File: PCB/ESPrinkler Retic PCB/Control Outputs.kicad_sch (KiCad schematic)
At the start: 0 parts

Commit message: Continue migrating PCB project to multi sheet design
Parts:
- added C1, C10, C11, C5, C6, C7, C8, C9: 12pF, symbol Device:C_Small
- added D1, D11, D14, D17, D22, D23, D24, D8: Generic_Triac_A1A2G, symbol Triac_Thyristor:Generic_Triac_A1A2G
- added D10, D13, D16, D19, D2, D20, D21, D7: D_TVS, symbol Device:D_TVS
- added D12, D15, D18, D25, D26, D27, D5, D9: LED, symbol Device:LED
- added Q1, Q10, Q4, Q5, Q6, Q7, Q8, Q9: Q_NMOS, symbol Device:Q_NMOS
- added R1, R17, R24, R31, R38, R49, R50, R51: 68R, symbol Device:R_Small
- added R15, R22, R29, R3, R36, R43, R44, R45: 120R, symbol Device:R_Small
- added R16, R2, R23, R30, R37, R46, R47, R48: 1.2k, symbol Device:R_Small
- added R18, R19, R25, R26, R32, R33, R39, R4, R40, R5, R52, R53, R54, R55, R56, R57: R, symbol Device:R
- added R20, R27, R34, R41, R58, R59, R6, R60: 10k, symbol Device:R
- added R21, R28, R35, R42, R61, R62, R63, R7: 1k, symbol Device:R
- added U1, U3, U4, U5, U6, U7, U8, U9: ~, symbol Relay_SolidState:MOC3063M
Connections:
- new net: D20.1 (A1), D23.2 (A2), R47.1
- new net: C10.1, R47.2, R50.1
- new net: D16.1 (A1), D17.2 (A2), R37.1
- new net: C11.1, R48.2, R51.1
- new net: C11.2, D24.1 (A1), R45.1
- new net: Q7.G, R41.2, R42.2
- new net: C9.2, D22.1 (A1), R43.1
- new net: D19.1 (A1), D22.2 (A2), R46.1
- new net: D22.3 (G), R43.2, U7.4
- new net: R19.2, U3.1
- new net: D18.2 (A), R39.2
- new net: Q10.G, R60.2, R63.2
- new net: R53.2, U7.1
- new net: D25.1 (K), Q8.S, U7.2
- new net: R49.2, U7.6
- new net: R33.2, U5.1
- new net: R40.2, U6.1
- new net: D18.1 (K), Q7.S, U6.2
- new net: D17.3 (G), R36.2, U6.4
- new net: R38.2, U6.6
- new net: D15.1 (K), Q6.S, U5.2
- new net: D14.3 (G), R29.2, U5.4
- new net: R31.2, U5.6
- new net: D12.2 (A), R25.2
- new net: C6.1, R23.2, R24.1
- new net: R24.2, U4.6
- new net: R4.2, U1.1
- new net: C6.2, D11.1 (A1), R22.1
- new net: D11.3 (G), R22.2, U4.4
- new net: D5.1 (K), Q1.S, U1.2
- new net: D1.3 (G), R3.2, U1.4
- new net: R1.2, U1.6
- new net: C10.2, D23.1 (A1), R44.1
- new net: Q4.G, R20.2, R21.2
- new net: D9.1 (K), Q4.S, U3.2
- new net: Q5.G, R27.2, R28.2
- new net: D7.1 (A1), D8.2 (A2), R16.1
- new net: C5.1, R16.2, R17.1
- new net: R51.2, U9.6
- new net: D23.3 (G), R44.2, U8.4
- new net: D27.1 (K), Q10.S, U9.2
- new net: D10.1 (A1), D11.2 (A2), R23.1
- new net: Q6.G, R34.2, R35.2
- new net: D1.2 (A2), D2.1 (A1), R2.1
- new net: C1.1, R1.1, R2.2
- new net: C9.1, R46.2, R49.1
- new net: C7.2, D14.1 (A1), R29.1
- new net: D13.1 (A1), D14.2 (A2), R30.1
- new net: Q1.G, R6.2, R7.2
- new net: R26.2, U4.1
- new net: Q8.G, R58.2, R61.2
- new net: D27.2 (A), R56.2
- new net: D26.1 (K), Q9.S, U8.2
- new net: D26.2 (A), R54.2
- new net: D15.2 (A), R32.2
- new net: D25.2 (A), R52.2
- new net: R57.2, U9.1
- new net: C5.2, D8.1 (A1), R15.1
- new net: D8.3 (G), R15.2, U3.4
- new net: C1.2, D1.1 (A1), R3.1
- new net: Q9.G, R59.2, R62.2
- new net: R55.2, U8.1
- new net: C7.1, R30.2, R31.1
- new net: D9.2 (A), R18.2
- new net: D5.2 (A), R5.2
- new net: D12.1 (K), Q5.S, U4.2
- new net: R17.2, U3.6
- new net: C8.1, R37.2, R38.1
- new net: R50.2, U8.6
- new net: C8.2, D17.1 (A1), R36.1
- new net: D21.1 (A1), D24.2 (A2), R48.1
- new net: D24.3 (G), R45.2, U9.4
- new net +5V: R18.1, R19.1, R25.1, R26.1, R32.1, R33.1, R39.1, R4.1, R40.1, R5.1, R52.1, R53.1, R54.1, R55.1, R56.1, R57.1
- new net GND: Q1.D, Q10.D, Q4.D, Q5.D, Q6.D, Q7.D, Q8.D, Q9.D, R20.1, R27.1, R34.1, R41.1, R58.1, R59.1, R6.1, R60.1
- new net LIVE: D10.2 (A2), D13.2 (A2), D16.2 (A2), D19.2 (A2), D2.2 (A2), D20.2 (A2), D21.2 (A2), D7.2 (A2)
- new net Pump: R21.1, R28.1, R35.1, R42.1, R61.1, R62.1, R63.1, R7.1

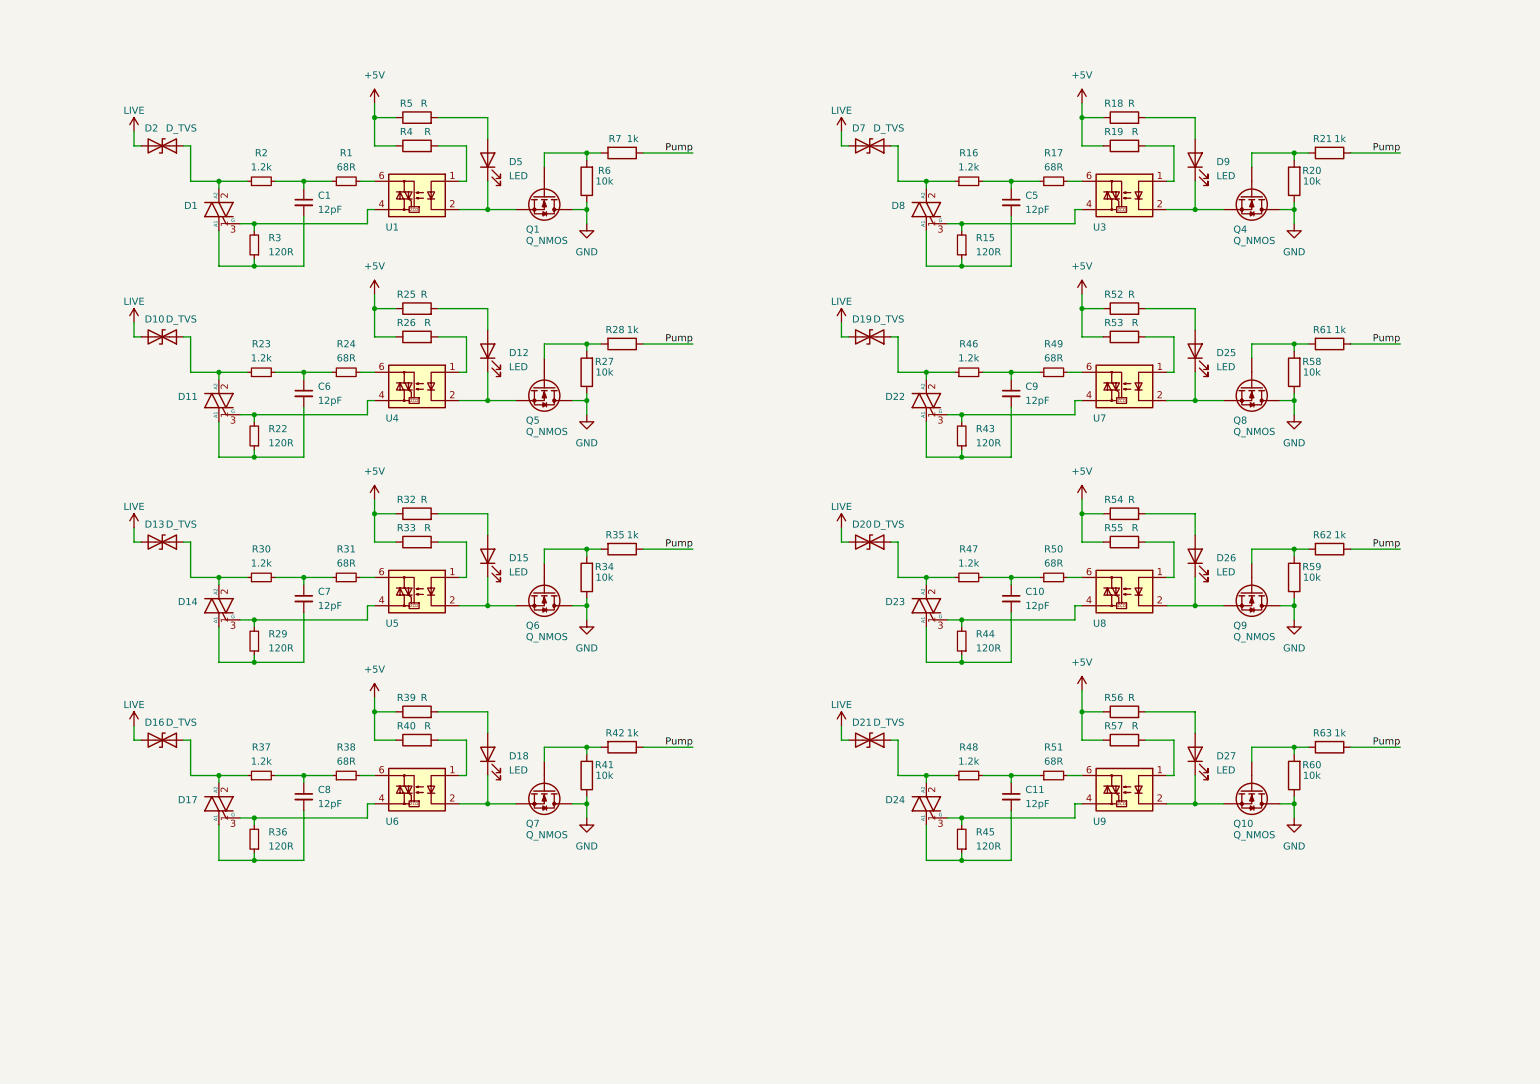
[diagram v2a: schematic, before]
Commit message: Lay out control schematic and begin choosing parts
Source parts for existing symbols on the control schematic after laying out pump and zone circuits
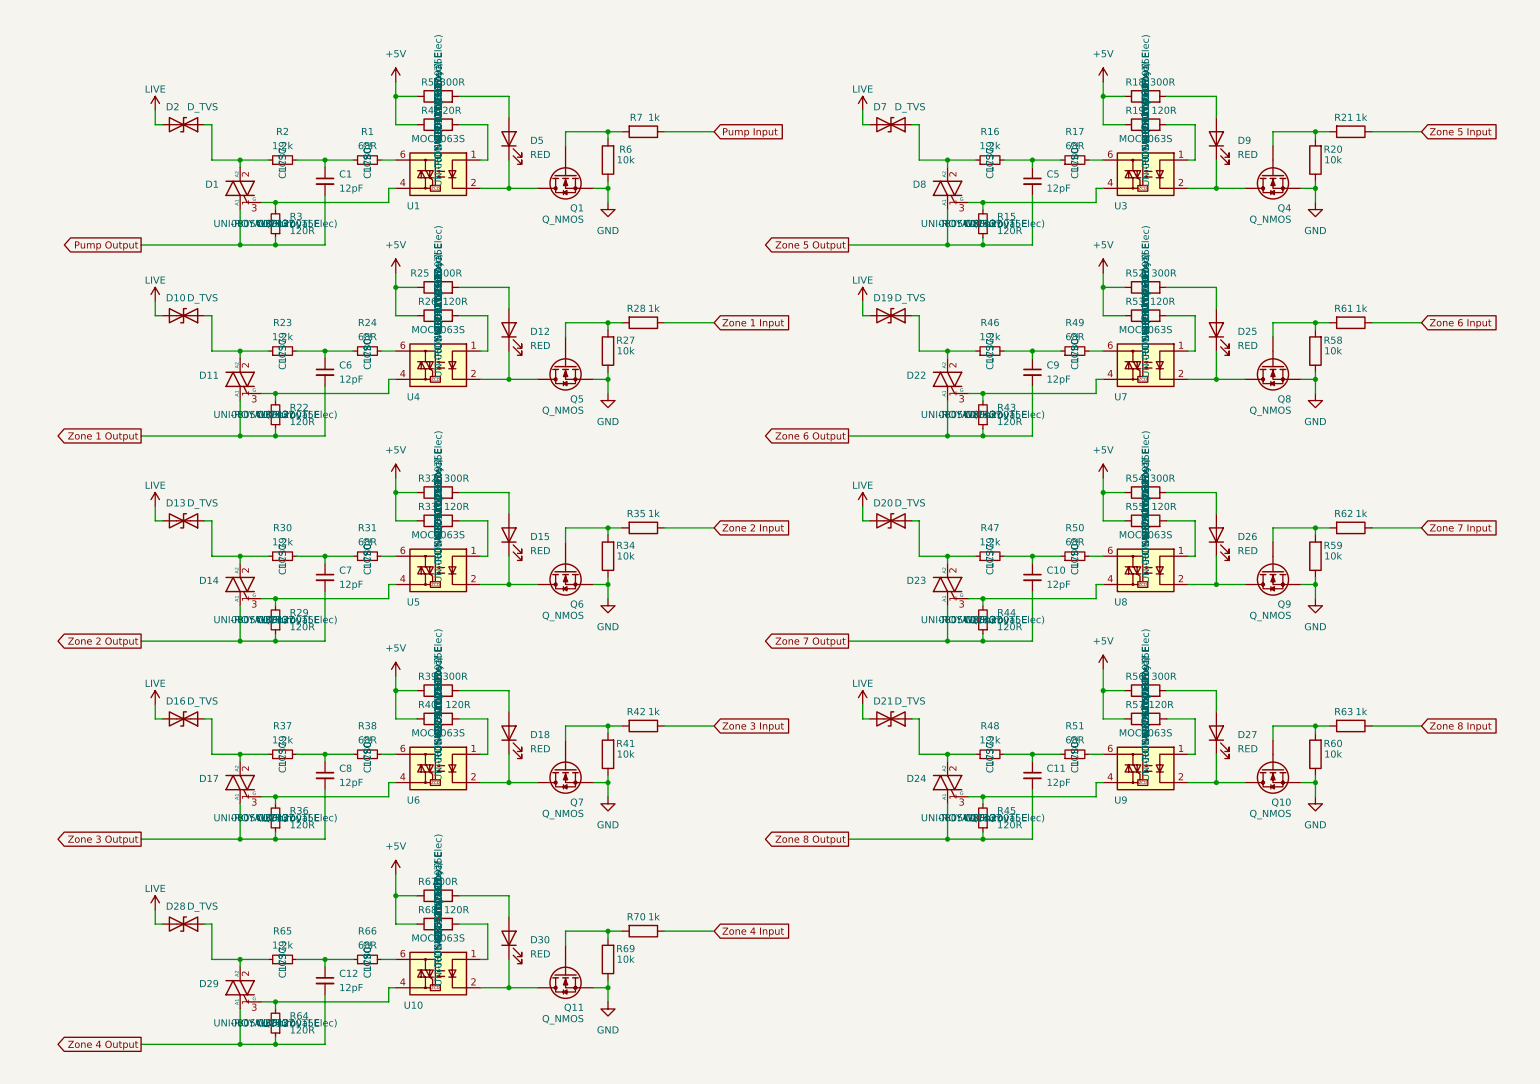
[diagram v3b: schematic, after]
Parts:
- added C12: 12pF, symbol Device:C_Small
- added D28: D_TVS, symbol Device:D_TVS
- added D29: Generic_Triac_A1A2G, symbol Triac_Thyristor:Generic_Triac_A1A2G
- added D30: RED, LED_SMD:LED_0603_1608Metric, symbol Device:LED
- added Q11: Q_NMOS, symbol Device:Q_NMOS
- added R64: 120R, Resistor_SMD:R_0805_2012Metric, symbol Device:R_Small
- added R65: 1.2k, symbol Device:R_Small
- added R66: 68R, symbol Device:R_Small
- added R67: 300R, Resistor_SMD:R_0805_2012Metric, symbol Device:R
- added R68: 120R, Resistor_SMD:R_0805_2012Metric, symbol Device:R
- added R69: 10k, symbol Device:R
- added R70: 1k, symbol Device:R
- added U10: MOC3063S, Package_SO:SOP-8_6.605x9.655mm_P2.54mm, symbol Relay_SolidState:MOC3063M
- D12, D15, D18, D25, D26, D27, D5, D9: value LED -> RED; footprint (none) -> LED_SMD:LED_0603_1608Metric; Manufacturer (none) -> Hubei KENTO Elec; Manufacturer P/N (none) -> KT-0603R; Supplier (none) -> LCSC; Supplier P/N (none) -> C2286
- R1, R17, R24, R31, R38, R49, R50, R51: Supplier (none) -> LCSC; Supplier P/N (none) -> C17802
- R15, R22, R29, R3, R36, R43, R44, R45: footprint (none) -> Resistor_SMD:R_0805_2012Metric; Manufacturer (none) -> UNI-ROYAL(Uniroyal Elec); Manufacturer P/N (none) -> 0805W8F1200T5E; Supplier (none) -> LCSC; Supplier P/N (none) -> C17437
- R16, R2, R23, R30, R37, R46, R47, R48: Supplier (none) -> LCSC; Supplier P/N (none) -> C17379
- R18, R25, R32, R39, R5, R52, R54, R56: value R -> 300R; footprint (none) -> Resistor_SMD:R_0805_2012Metric; Manufacturer (none) -> UNI-ROYAL(Uniroyal Elec); Manufacturer P/N (none) -> 0805W8F3000T5E; Supplier (none) -> LCSC; Supplier P/N (none) -> C17617
- R19, R26, R33, R4, R40, R53, R55, R57: value R -> 120R; footprint (none) -> Resistor_SMD:R_0805_2012Metric; Manufacturer (none) -> UNI-ROYAL(Uniroyal Elec); Manufacturer P/N (none) -> 0805W8F1200T5E; Supplier (none) -> LCSC; Supplier P/N (none) -> C17437
- U1, U3, U4, U5, U6, U7, U8, U9: value ~ -> MOC3063S; footprint (none) -> Package_SO:SOP-8_6.605x9.655mm_P2.54mm; Manufacturer (none) -> Lite-On; Manufacturer P/N (none) -> MOC3063S-TA1; Supplier (none) -> LCSC; Supplier P/N (none) -> C77950
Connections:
- net +5V: now also R67.1, R68.1
- net GND: now also Q1.S, Q10.S, Q4.S, Q5.S, Q6.S, Q7.S, Q8.S, Q9.S, Q11.S, R69.1; no longer Q1.D, Q10.D, Q4.D, Q5.D, Q6.D, Q7.D, Q8.D, Q9.D
- net LIVE: now also D28.2 (A2)
- net Zone 8 Output: now reaches C11.2, D24.1 (A1), R45.1
- net Zone 6 Output: now reaches C9.2, D22.1 (A1), R43.1
- net at D25.1 (K), U7.2: now also Q8.D; no longer Q8.S
- net at D18.1 (K), U6.2: now also Q7.D; no longer Q7.S
- net at D15.1 (K), U5.2: now also Q6.D; no longer Q6.S
- net Zone 1 Output: now reaches C6.2, D11.1 (A1), R22.1
- net at D5.1 (K), U1.2: now also Q1.D; no longer Q1.S
- net Zone 7 Output: now reaches C10.2, D23.1 (A1), R44.1
- net at D9.1 (K), U3.2: now also Q4.D; no longer Q4.S
- net at D27.1 (K), U9.2: now also Q10.D; no longer Q10.S
- net Zone 2 Output: now reaches C7.2, D14.1 (A1), R29.1
- net at D26.1 (K), U8.2: now also Q9.D; no longer Q9.S
- net Zone 5 Output: now reaches C5.2, D8.1 (A1), R15.1
- net Pump Output: now reaches C1.2, D1.1 (A1), R3.1
- net at D12.1 (K), U4.2: now also Q5.D; no longer Q5.S
- net Zone 3 Output: now reaches C8.2, D17.1 (A1), R36.1
- removed net Pump: R21.1, R28.1, R35.1, R42.1, R61.1, R62.1, R63.1, R7.1
- new net: R68.2, U10.1
- new net: D30.1 (K), Q11.D, U10.2
- new net: D29.3 (G), R64.2, U10.4
- new net: R66.2, U10.6
- new net: Q11.G, R69.2, R70.2
- new net: D28.1 (A1), D29.2 (A2), R65.1
- new net: D30.2 (A), R67.2
- new net: C12.1, R65.2, R66.1
- new net Pump Input: R7.1
- new net Zone 1 Input: R28.1
- new net Zone 2 Input: R35.1
- new net Zone 3 Input: R42.1
- new net Zone 4 Input: R70.1
- new net Zone 4 Output: C12.2, D29.1 (A1), R64.1
- new net Zone 5 Input: R21.1
- new net Zone 6 Input: R61.1
- new net Zone 7 Input: R62.1
- new net Zone 8 Input: R63.1
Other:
- moved on the sheet: C1, C10, C11, C5, C6, C7, C8, C9, D1, D10, D11, D12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

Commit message: Continue parts sourcing for existing components
Continue to source parts from LCSC for the existing components.
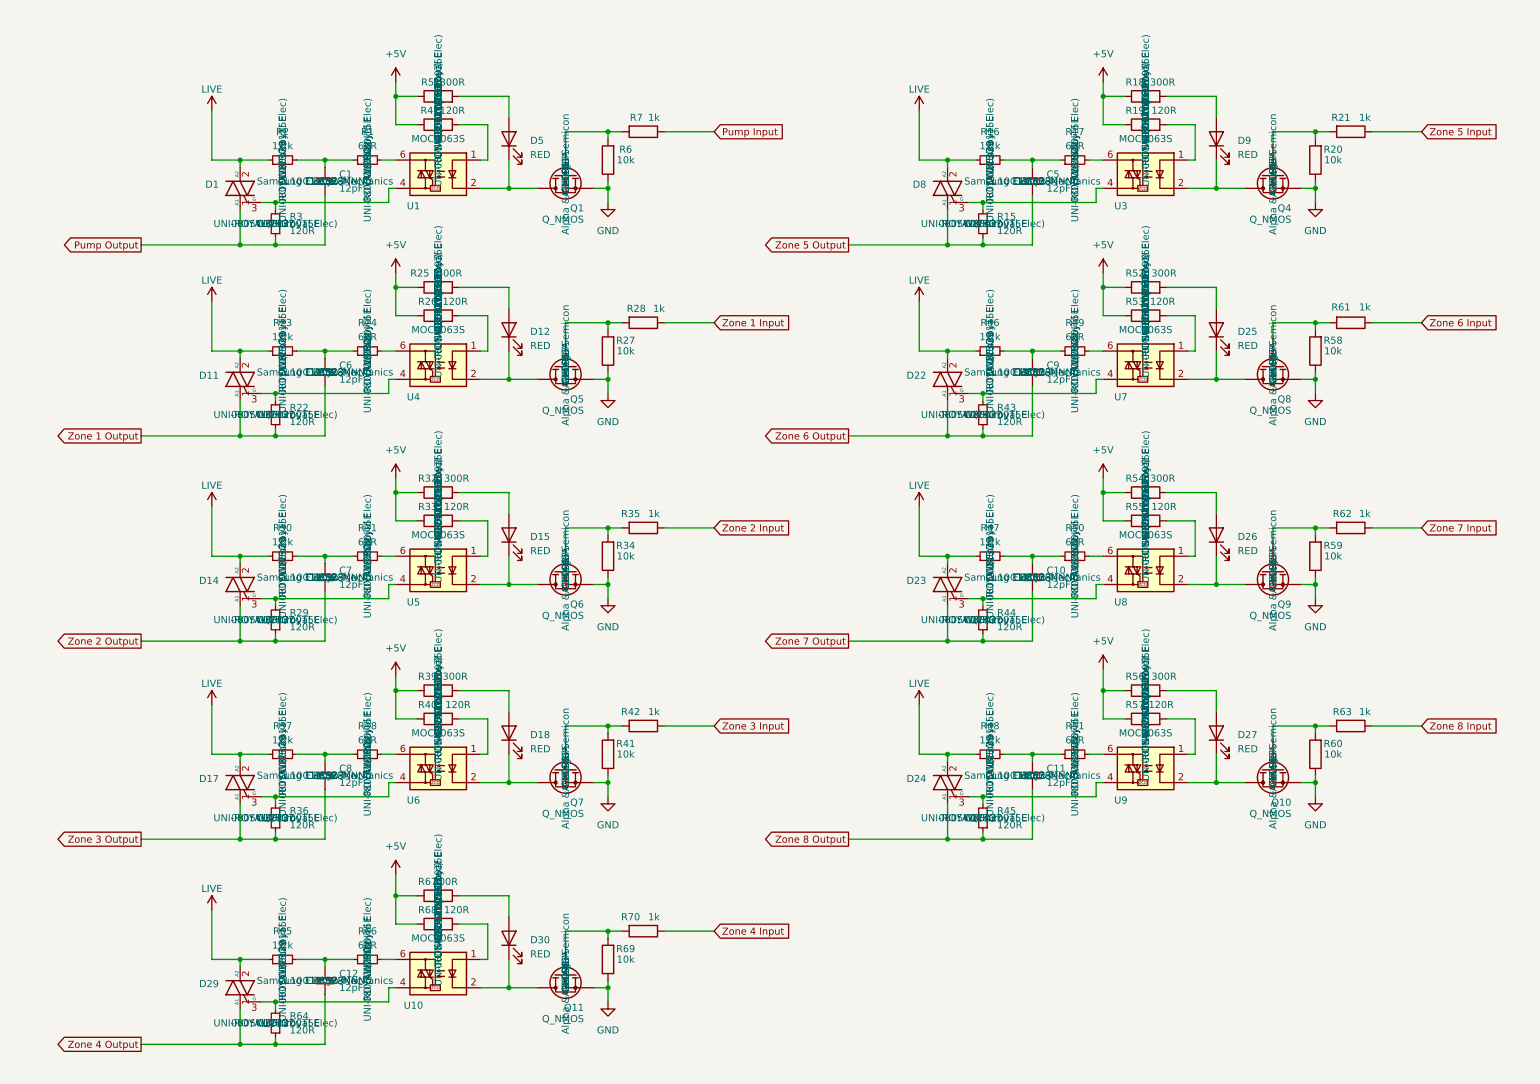
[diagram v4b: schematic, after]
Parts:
- removed D10, D13, D16, D19, D2, D20, D21, D28, D7: D_TVS, symbol Device:D_TVS
- C1, C10, C11, C12, C5, C6, C7, C8, C9: footprint (none) -> Capacitor_SMD:C_0603_1608Metric; Manufacturer (none) -> Samsung Electro-Mechanics; Manufacturer P/N (none) -> CL10C120JB8NNNC; Supplier (none) -> LCSC; Supplier P/N (none) -> C38523
- Q1, Q10, Q11, Q4, Q5, Q6, Q7, Q8, Q9: footprint (none) -> Package_TO_SOT_SMD:SOT-23_Handsoldering; Manufacturer (none) -> Alpha & Omega Semicon; Manufacturer P/N (none) -> AO3400A; Supplier (none) -> LCSC; Supplier P/N (none) -> C20917
- R1, R17, R24, R31, R38, R49, R50, R51, R66: footprint (none) -> Resistor_SMD:R_0805_2012Metric; Manufacturer (none) -> UNI-ROYAL(Uniroyal Elec); Manufacturer P/N (none) -> 0805W8F680JT5E
- R16, R2, R23, R30, R37, R46, R47, R48, R65: footprint (none) -> Resistor_SMD:R_0805_2012Metric; Manufacturer (none) -> UNI-ROYAL(Uniroyal Elec); Manufacturer P/N (none) -> 0805W8F1201T5E
- R20, R27, R34, R41, R58, R59, R6, R60, R69: footprint (none) -> Resistor_SMD:R_0805_2012Metric; Manufacturer (none) -> UNI-ROYAL(Uniroyal Elec); Manufacturer P/N (none) -> 0805W8F1002T5E; Supplier (none) -> LCSC; Supplier P/N (none) -> C17414
- R21, R28, R35, R42, R61, R62, R63, R7, R70: footprint (none) -> Resistor_SMD:R_0805_2012Metric; Manufacturer (none) -> UNI-ROYAL(Uniroyal Elec); Manufacturer P/N (none) -> 0805W8F1001T5E; Supplier (none) -> LCSC; Supplier P/N (none) -> C17513
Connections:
- net LIVE: now also D1.2 (A2), D11.2 (A2), D14.2 (A2), D17.2 (A2), D22.2 (A2), D23.2 (A2), D24.2 (A2), D29.2 (A2), D8.2 (A2), R16.1, R2.1, R23.1, R30.1, R37.1, R46.1, R47.1, R48.1, R65.1
